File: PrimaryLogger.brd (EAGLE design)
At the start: 52.1 x 77.1 mm, 55 parts, among them J1 CONN_42.54_SCREW, J2 CONN_42.54_SCREW, J3 CONN_42.54_SCREW, J4 CONN_42.54_SCREW, J5 CONN_32.54_SCREW, Q1 DMG3404, Q2 DMG3404, U1 MIC2005, U2 MIC2091, U25 SN74AUP3G34DCU, U3 TPL5010DDC, U4 TXS0102DCU, U5 SN74LVC1G3157DRL, U6 TCS3400, U7 SHTC3DFN, U8 MCP23008QFN, U9 MCP7940SOIC

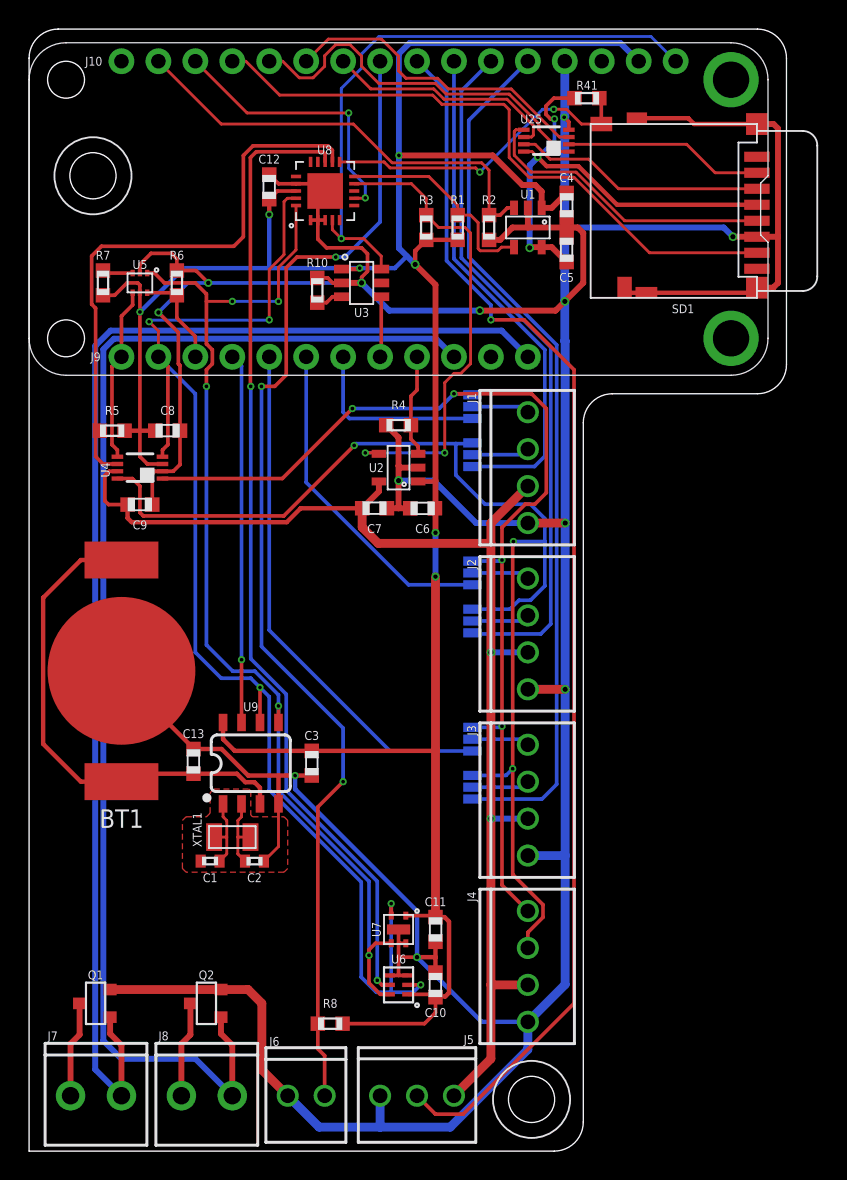
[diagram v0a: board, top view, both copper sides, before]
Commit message: Minor updates to layout
Added silk screen, added test points, other minor edits
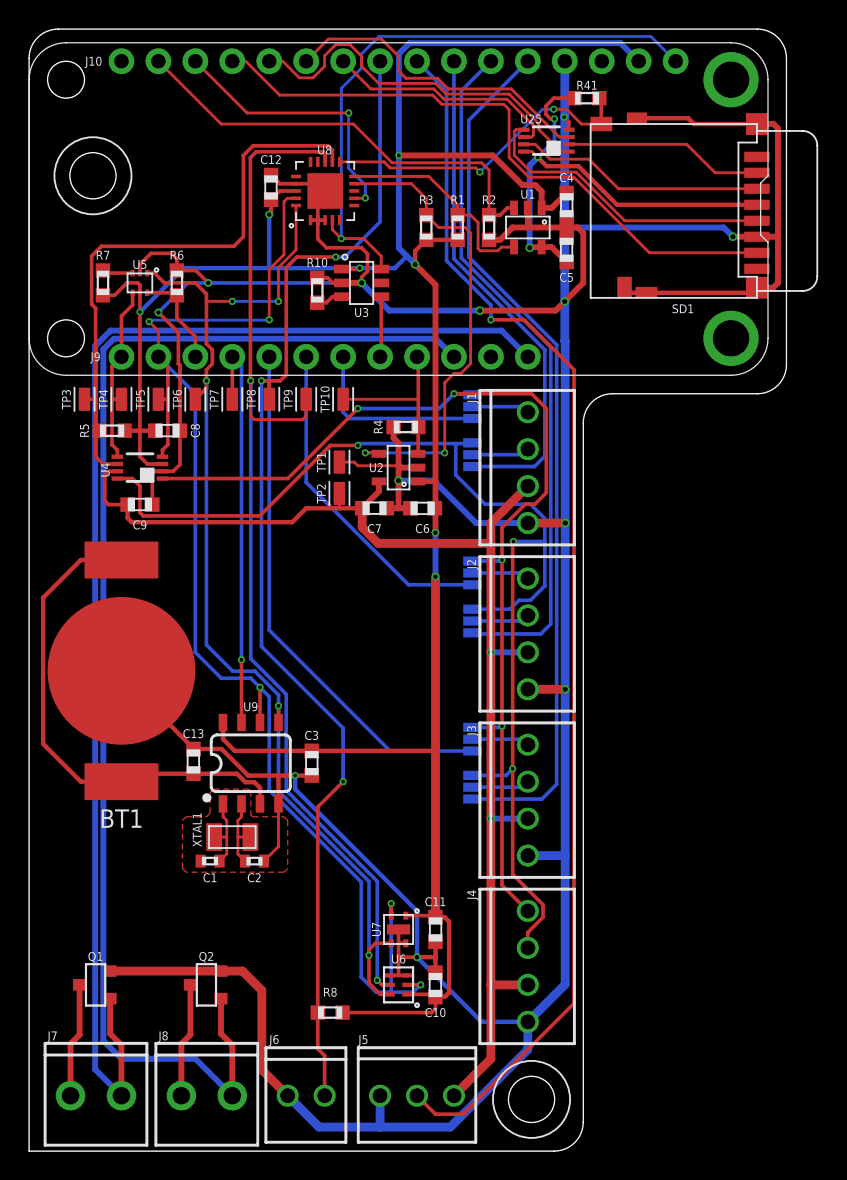
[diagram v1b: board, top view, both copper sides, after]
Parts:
- added TP1, TP10, TP2, TP3, TP4, TP5, TP6, TP7, TP8, TP9: TESTPOINTRCU, bschulz:TESTPOINT_0603
- C13: value (none) -> 0.1uF
- moved Q1 1.27 mm to (4.57, 11.4)
- moved Q2 1.27 mm to (12.2, 11.4)
- moved R8 0.76 mm to (20.7, 9.53)
- moved R4 0.52 mm to (25.9, 49.8)
- moved C12 0.13 mm to (16.6, 66.3)
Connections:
- net 3V3_EXT: now also TP2.1
- net 3V3_EXT_EN: now also TP10.1
- net GND: now also TP1.1
- net I2C_EXT_EN: now also TP3.1
- net PAR_INT: now also TP9.1
- net RTC_INT: now also TP7.1
- net SCL: now also TP5.1
- net SDA: now also TP4.1
- net SDA_OB: now also TP6.1
- net TIP: now also TP8.1
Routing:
- net PAR_INT: track 67.1 -> 74.6 mm
- net 3V3_EXT_EN: track 7.16 -> 12.1 mm
- net GND: track 326.0 -> 330.7 mm
- net RTC_INT: track 25.4 -> 28.3 mm
- net SDA_OB: track 74.9 -> 76.5 mm
- net TIP: track 80.2 -> 81.7 mm
- net VSYS-: track 6.61 -> 7.88 mm
- net VBAT-: track 6.61 -> 7.88 mm
- net VBUS_FEATHER: track 88.6 -> 89.9 mm
- net VBAT_FEATHER: track 88.9 -> 90.2 mm
- net 3V3_EXT: track 86.5 -> 87.6 mm
- net I2C_EXT_EN: track 39.8 -> 40.6 mm
- net SCL: track 92.3 -> 93.0 mm
- net SDA: track 12.0 -> 12.7 mm
- net 3V3: track 179.0 -> 178.4 mm
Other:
- board text added: "3v3"
- board text added: "5v In"
- board text added: "BAT+"
- board text added: "BAT-"
- board text added: "Bat In\"
- board text added: "D1"
- board text added: "D2"
- board text added: "D3"
- board text added: "D4"
- board text added: "D5"
- board text added: "D6"
- board text added: "GND"
- board text added: "I2C In"
- board text added: "P1"
- board text added: "Pot In"
- board text added: "Project Hyena v0.0 Bobby Schulz UMN/GEMS"
- board text added: "SCL"
- board text added: "SDA"
- board text added: "SYS+"
- board text added: "SYS-"
- board text added: "Sense In"
- board text added: "TIP"
- board text added: "Tip In"

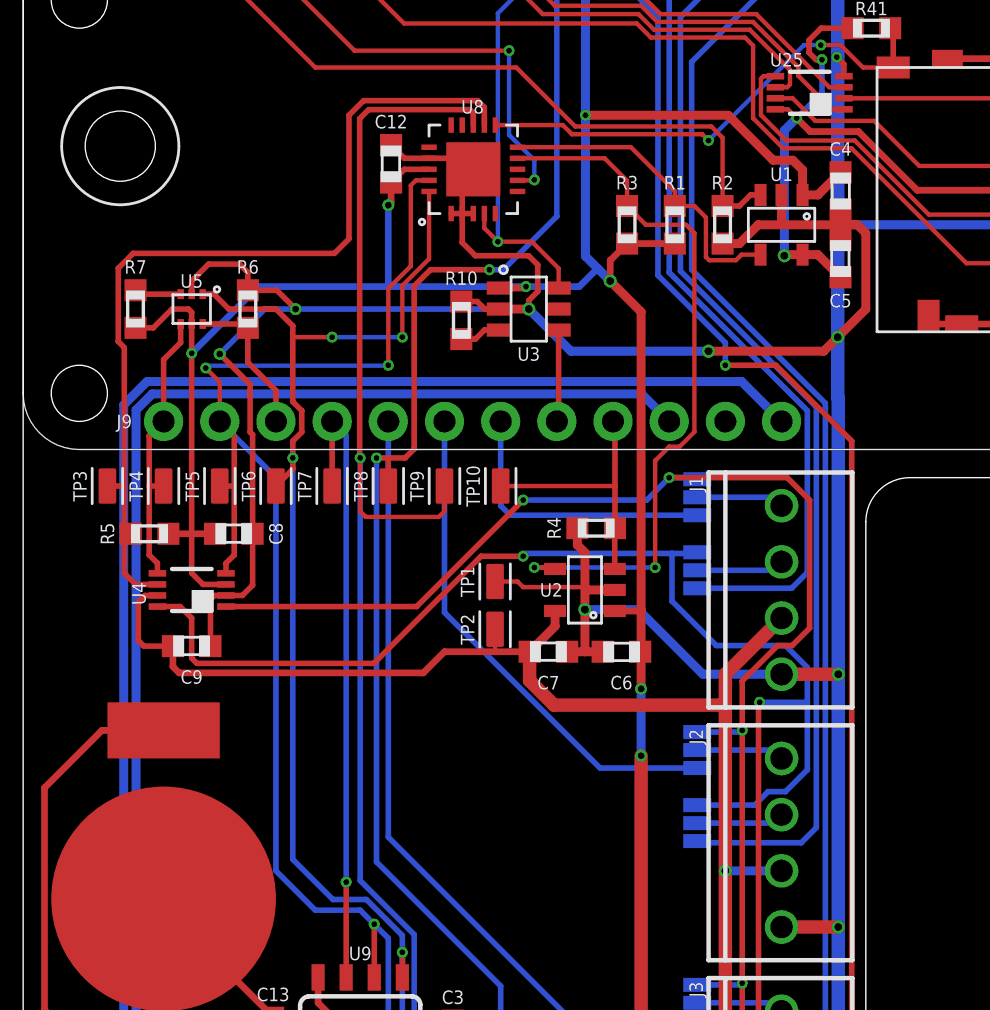
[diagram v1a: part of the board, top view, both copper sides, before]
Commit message: Minor updates to make consistent with Soil Symbiont
Changed 10uF to 0805 and mux to SC-70 package
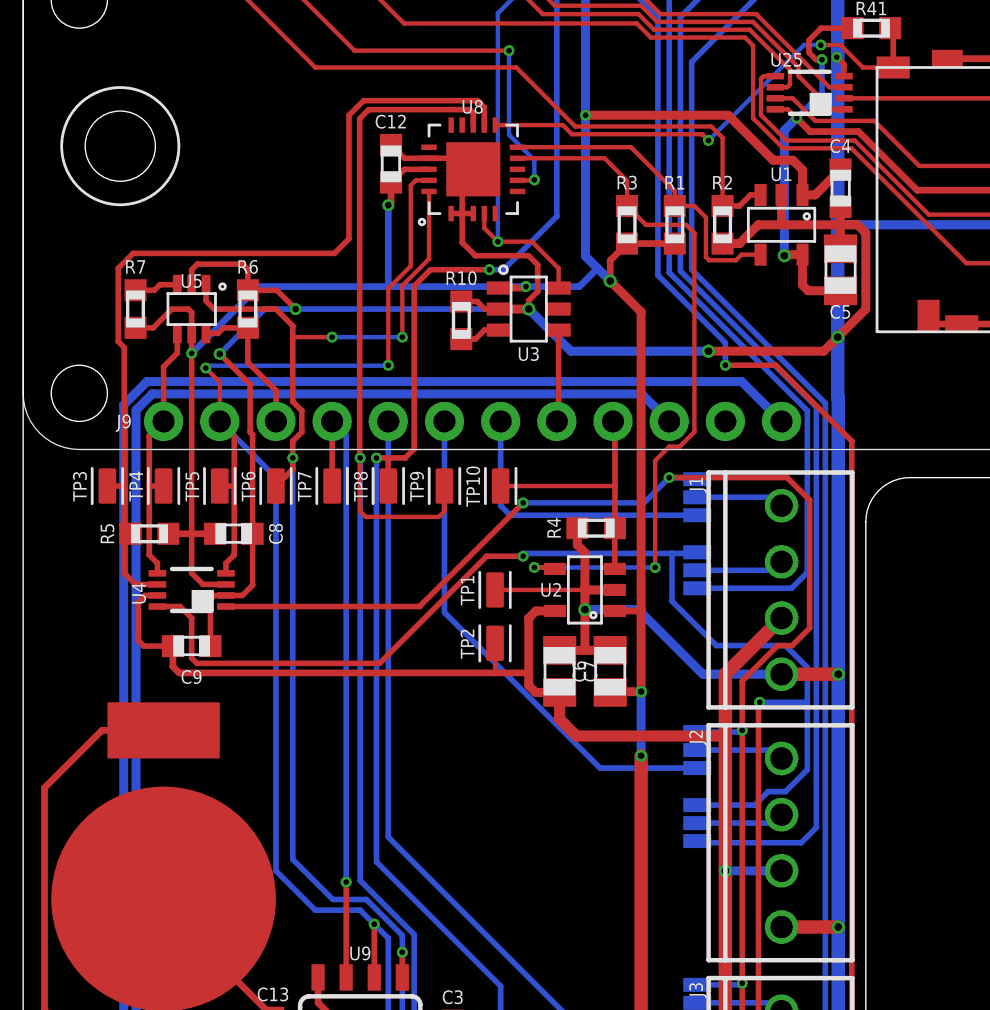
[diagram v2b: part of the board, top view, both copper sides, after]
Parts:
- C5, C6, C7: device bschulz_passives:C0603 -> bschulz_passives:C0805
- U5: value SN74LVC1G3157DRL -> SN74LVC1G3157SC70; device bschulz:DRL_R-PDSO-N6 -> bschulz:DCK_R-PDSO-G6
- moved C7 1.02 mm to (24.3, 43.3), turned to 90 degrees
- moved C6 1.02 mm to (26.5, 43.3), turned to 90 degrees
- moved TP2 0.64 mm to (21.3, 44.6)
- moved C5 0.51 mm to (37.0, 61.5)
- moved TP1 0.38 mm to (21.3, 47.0)
- moved C4 0.13 mm to (37.0, 65.2)
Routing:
- net 3V3_EXT: track 87.6 -> 89.4 mm
- net 3V3: track 178.4 -> 179.7 mm
- net 3V3_SD: track 33.6 -> 34.6 mm
- net GND: track 330.7 -> 331.7 mm
